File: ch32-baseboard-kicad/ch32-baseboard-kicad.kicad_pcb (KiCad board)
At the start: 4 copper layers, 55 x 36 mm, 49 parts, among them J1 USB_C_USB2.0_16P, J2 TC2030, J3 53048-0310, SW1 SW_DIP_x02, SW2 TS-1088, U1 CH32V30xRxTx, U2 SPX3819M5-L-3-3, U3 INA195, X1 16MHz

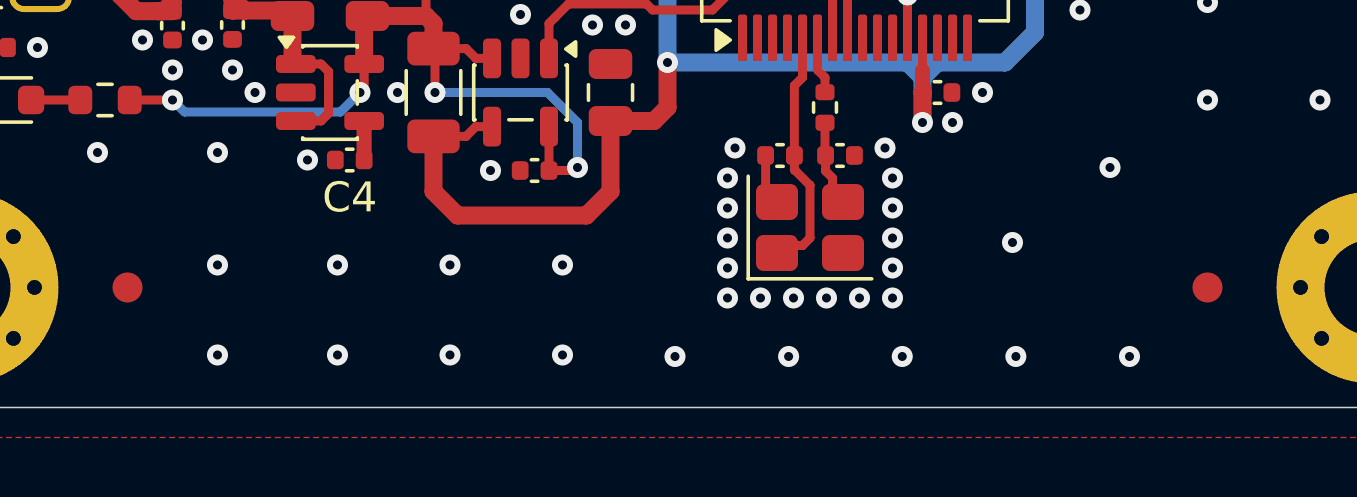
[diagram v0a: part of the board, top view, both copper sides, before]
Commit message: feat: silkscreen updates, manufacturing files
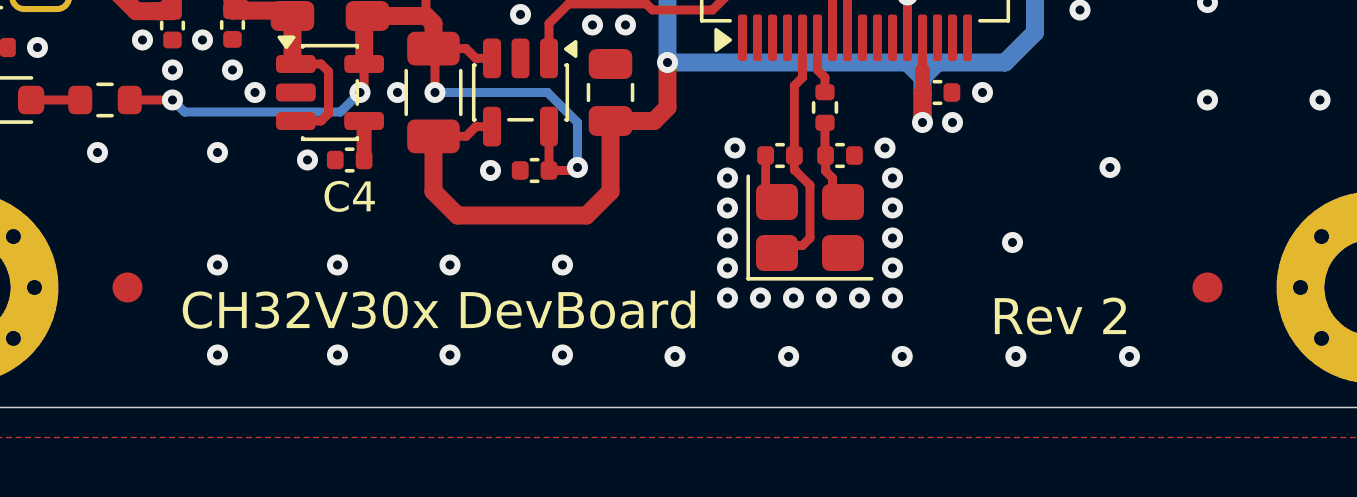
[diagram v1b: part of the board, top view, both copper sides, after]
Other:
- board text added: "CH32V30x DevBoard"
- board text added: "Rev 2"
